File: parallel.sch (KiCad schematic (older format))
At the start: 11 parts, among them J11 Conn_02x13_Header, U5 MCP23S17_SP

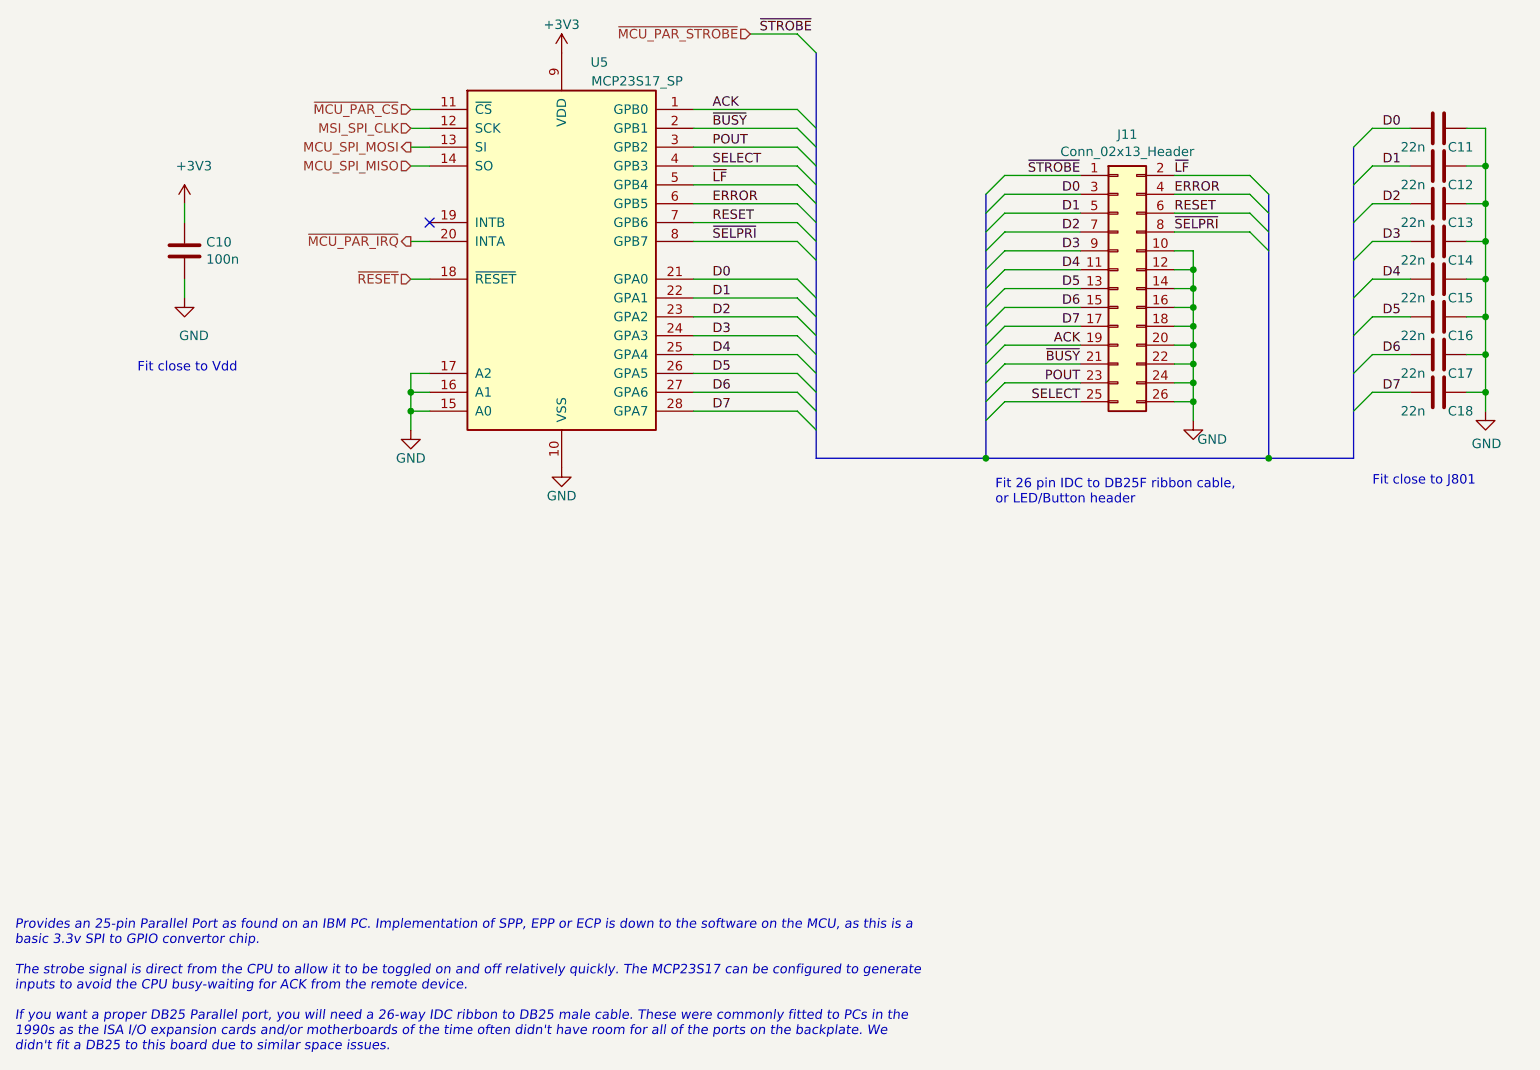
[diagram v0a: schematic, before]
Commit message: Cleaned up Atmega reset. Set hold size to 3.5mm, so M3 screws go through nicely Reset numbering to page x 100 Renamed Launchpad to EK-TM4C123GXL Renamed top-level signals to KBMS page as KBMS_TO/FROM_MCU
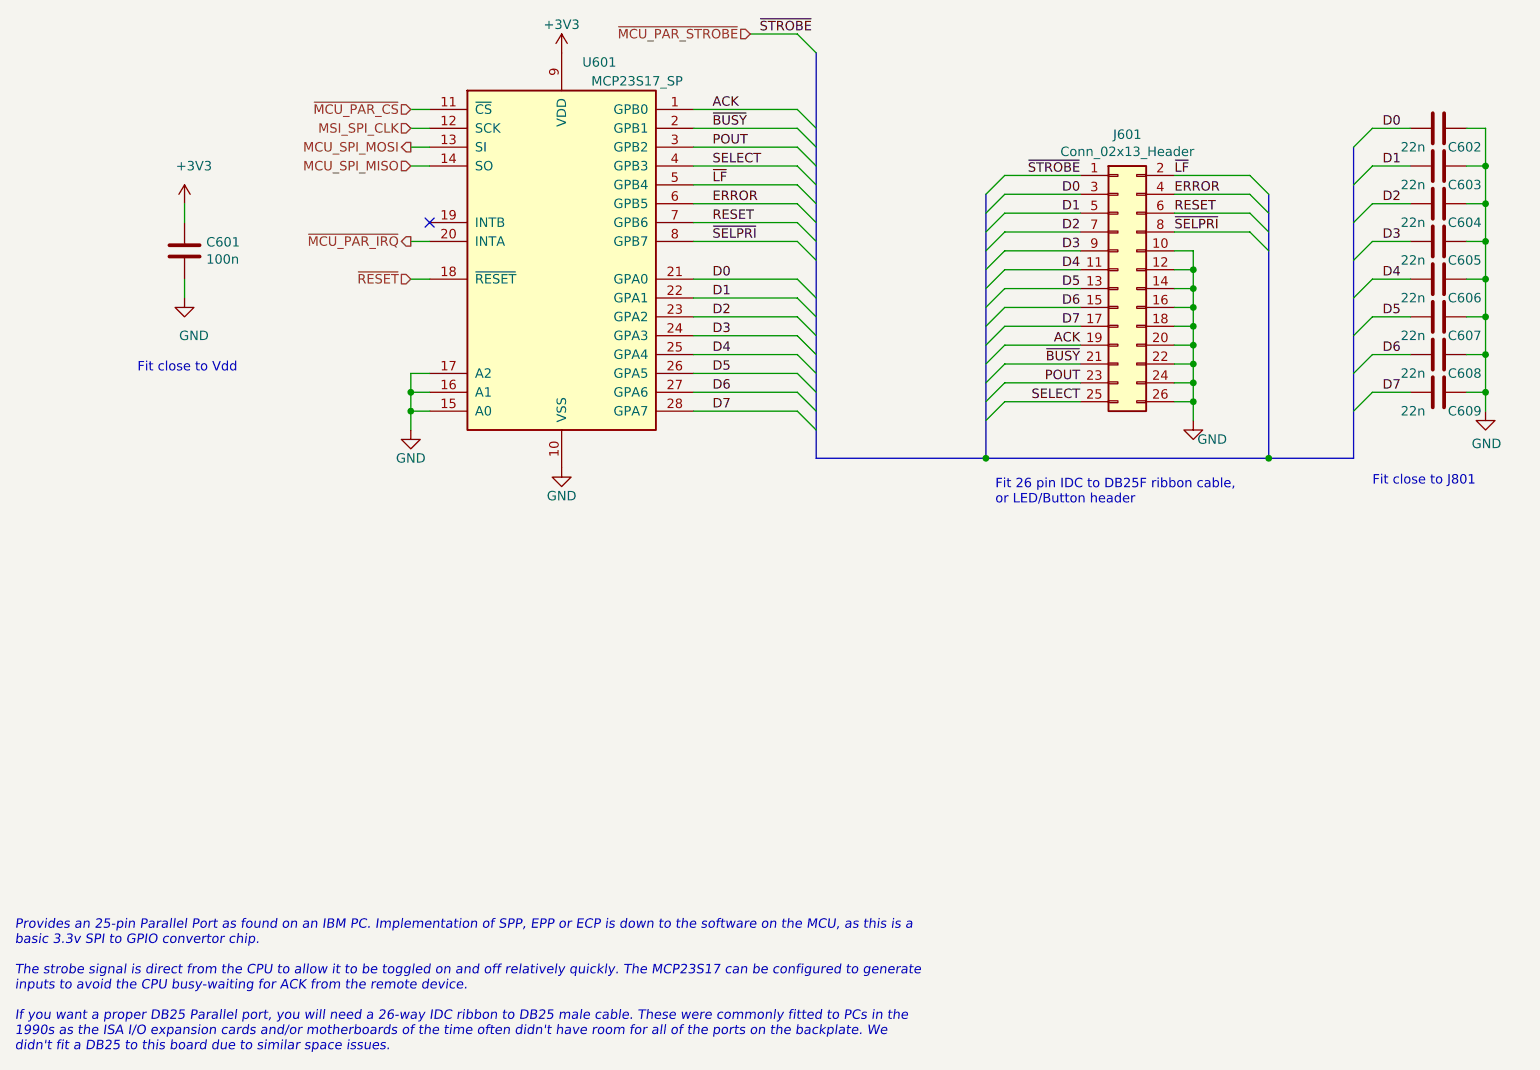
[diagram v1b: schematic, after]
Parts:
- renumbered C10 to C601, C11 to C602, C12 to C603, C13 to C604, C14 to C605, C15 to C606, C16 to C607, C17 to C608, C18 to C609, J11 to J601, U5 to U601
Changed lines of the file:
@@
 P 3450 3500
 AR Path="/5DF2345B/5DF6E091" Ref="U?"  Part="1"
-AR Path="/5DF626CD/5DF6E091" Ref="U5"  Part="1"
-F 0 "U5" H 3650 4550 50  0000 C CNN
+AR Path="/5DF626CD/5DF6E091" Ref="U601"  Part="1"
+F 0 "U601" H 3650 4550 50  0000 C CNN
 F 1 "MCP23S17_SP" H 3850 4450 50  0000 C CNN
 F 2 "Package_DIP:DIP-28_W7.62mm" H 3650 2500 50  0001 L CNN
@@
 $EndComp
 $Comp
-L Device:C C11
+L Device:C C602
 U 1 1 5DFC954B
 P 8100 2800
-F 0 "C11" V 8200 2850 50  0000 L CNN
+F 0 "C602" V 8200 2850 50  0000 L CNN
 F 1 "22n" V 8200 2600 50  0000 L CNN
 F 2 "Capacitor_THT:C_Disc_D3.0mm_W2.0mm_P2.50mm" H 8138 2650 50  0001 C CNN
@@
 $EndComp
 $Comp
-L Device:C C18
+L Device:C C609
 U 1 1 5DFC9175
 P 8100 4200
-F 0 "C18" V 8200 4250 50  0000 L CNN
+F 0 "C609" V 8200 4250 50  0000 L CNN
 F 1 "22n" V 8200 4000 50  0000 L CNN
 F 2 "Capacitor_THT:C_Disc_D3.0mm_W2.0mm_P2.50mm" H 8138 4050 50  0001 C CNN
@@
 $EndComp
 $Comp
-L Device:C C12
+L Device:C C603
 U 1 1 5DFC8D43
 P 8100 3000
-F 0 "C12" V 8200 3050 50  0000 L CNN
+F 0 "C603" V 8200 3050 50  0000 L CNN
 F 1 "22n" V 8200 2800 50  0000 L CNN
 F 2 "Capacitor_THT:C_Disc_D3.0mm_W2.0mm_P2.50mm" H 8138 2850 50  0001 C CNN
@@
 $EndComp
 $Comp
-L Device:C C13
+L Device:C C604
 U 1 1 5DFC8AB4
 P 8100 3200
-F 0 "C13" V 8200 3250 50  0000 L CNN
+F 0 "C604" V 8200 3250 50  0000 L CNN
 F 1 "22n" V 8200 3000 50  0000 L CNN
 F 2 "Capacitor_THT:C_Disc_D3.0mm_W2.0mm_P2.50mm" H 8138 3050 50  0001 C CNN
@@
 $EndComp
 $Comp
-L Device:C C14
+L Device:C C605
 U 1 1 5DFC872D
 P 8100 3400
-F 0 "C14" V 8200 3450 50  0000 L CNN
+F 0 "C605" V 8200 3450 50  0000 L CNN
 F 1 "22n" V 8200 3200 50  0000 L CNN
 F 2 "Capacitor_THT:C_Disc_D3.0mm_W2.0mm_P2.50mm" H 8138 3250 50  0001 C CNN
@@
 $EndComp
 $Comp
-L Device:C C17
+L Device:C C608
 U 1 1 5DFC842B
 P 8100 4000
-F 0 "C17" V 8200 4050 50  0000 L CNN
+F 0 "C608" V 8200 4050 50  0000 L CNN
 F 1 "22n" V 8200 3800 50  0000 L CNN
 F 2 "Capacitor_THT:C_Disc_D3.0mm_W2.0mm_P2.50mm" H 8138 3850 50  0001 C CNN
@@
 $EndComp
 $Comp
-L Device:C C16
+L Device:C C607
 U 1 1 5DFC7FF4
 P 8100 3800
-F 0 "C16" V 8200 3850 50  0000 L CNN
+F 0 "C607" V 8200 3850 50  0000 L CNN
 F 1 "22n" V 8200 3600 50  0000 L CNN
 F 2 "Capacitor_THT:C_Disc_D3.0mm_W2.0mm_P2.50mm" H 8138 3650 50  0001 C CNN
@@
 $EndComp
 $Comp
-L Device:C C15
+L Device:C C606
 U 1 1 5DFC5D41
 P 8100 3600
-F 0 "C15" V 8200 3650 50  0000 L CNN
+F 0 "C606" V 8200 3650 50  0000 L CNN
 F 1 "22n" V 8200 3400 50  0000 L CNN
 F 2 "Capacitor_THT:C_Disc_D3.0mm_W2.0mm_P2.50mm" H 8138 3450 50  0001 C CNN
@@
 P 1450 3450
 AR Path="/5DF1D0B0/5E01C54F" Ref="C?"  Part="1"
-AR Path="/5DF626CD/5E01C54F" Ref="C10"  Part="1"
-F 0 "C10" H 1565 3496 50  0000 L CNN
+AR Path="/5DF626CD/5E01C54F" Ref="C601"  Part="1"
+F 0 "C601" H 1565 3496 50  0000 L CNN
 F 1 "100n" H 1565 3405 50  0000 L CNN
 F 2 "Capacitor_THT:C_Disc_D3.0mm_W2.0mm_P2.50mm" H 1488 3300 50  0001 C CNN
@@
 	1450 3600 1450 3700
 $Comp
-L Connector_Generic:Conn_02x13_Odd_Even J11
+L Connector_Generic:Conn_02x13_Odd_Even J601
 U 1 1 5DF553E8
 P 6400 3650
-F 0 "J11" H 6450 4467 50  0000 C CNN
+F 0 "J601" H 6450 4467 50  0000 C CNN
 F 1 "Conn_02x13_Header" H 6450 4376 50  0000 C CNN
 F 2 "Connector_IDC:IDC-Header_2x13_P2.54mm_Vertical" H 6400 3650 50  0001 C CNN
